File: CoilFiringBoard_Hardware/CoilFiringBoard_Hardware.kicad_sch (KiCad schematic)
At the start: 16 parts, among them Q1 Q_NMOS_GDS, Q2 Q_NMOS_GDS

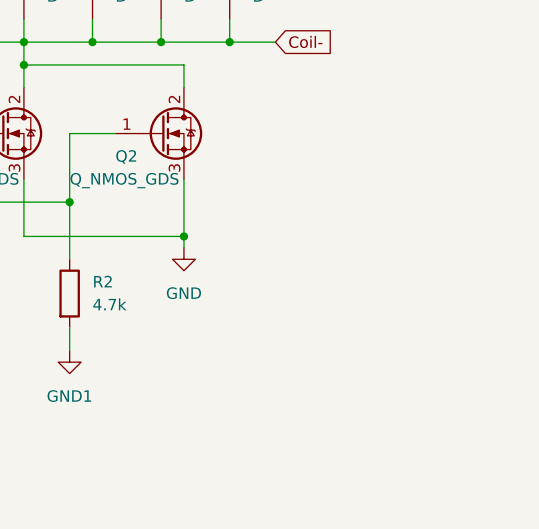
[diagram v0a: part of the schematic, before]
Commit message: Updated layout
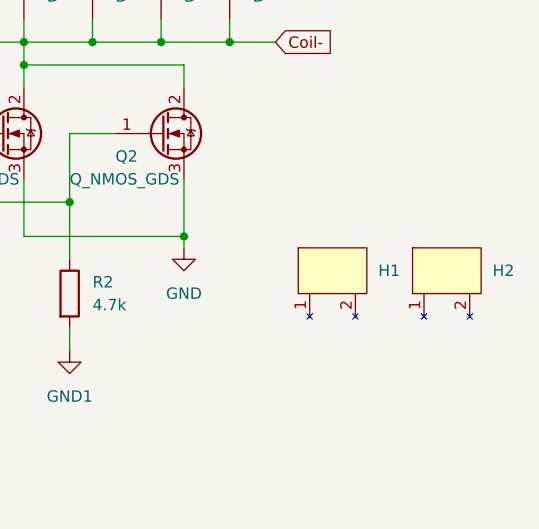
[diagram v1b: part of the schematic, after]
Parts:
- added H1, H2: ~, SeniorDesign:WV-T264-101E, symbol SeniorDesign:WV-T264-101E
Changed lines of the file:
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@@
+    )
+  )
+  (symbol (lib_id "SeniorDesign:WV-T264-101E") (at 180.34 99.06 0) (unit 1)
+    (in_bom yes) (on_board yes) (dnp no) (fields_autoplaced)
+    (property "Reference" "H1" (at 185.42 99.06 0)
+      (effects (font (size 1.27 1.27)) (justify left))
+    )
+    (property "Value" "~" (at 180.34 99.06 0)
+      (effects (font (size 1.27 1.27)))
+    )
+    (property "Footprint" "SeniorDesign:WV-T264-101E" (at 180.34 99.06 0)
+      (effects (font (size 1.27 1.27)) hide)
+    )
+    (property "Datasheet" "" (at 180.34 99.06 0)
+      (effects (font (size 1.27 1.27)) hide)
+    )
+    (pin "1")
+    (pin "2")
+    (instances
+      (project "CoilFiringBoard_Hardware"
+        (path "/28c13569-1eb8-4279-9ec4-13288f6f9832"
+          (reference "H1") (unit 1)
+        )
+      )
     )
   )
@@
         )
       )
+    )
+  )
+  (symbol (lib_id "SeniorDesign:WV-T264-101E") (at 193.04 99.06 0) (unit 1)
+    (in_bom yes) (on_board yes) (dnp no) (fields_autoplaced)
+    (property "Reference" "H2" (at 198.12 99.06 0)
+      (effects (font (size 1.27 1.27)) (justify left))
+    )
+    (property "Value" "~" (at 193.04 99.06 0)
+      (effects (font (size 1.27 1.27)))
+    )
+    (property "Footprint" "SeniorDesign:WV-T264-101E" (at 193.04 99.06 0)
+      (effects (font (size 1.27 1.27)) hide)
+    )
+    (property "Datasheet" "" (at 193.04 99.06 0)
+      (effects (font (size 1.27 1.27)) hide)
+    )
+    (pin "1")
+    (pin "2")
+    (instances
+      (project "CoilFiringBoard_Hardware"
+        (path "/28c13569-1eb8-4279-9ec4-13288f6f9832"
+          (reference "H2") (unit 1)
+        )
+      )

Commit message: Changed cap footprint
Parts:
- C1: footprint Capacitor_THT:C_Disc_D10.5mm_W5.0mm_P10.00mm -> Capacitor_THT:C_Rect_L13.0mm_W5.0mm_P10.00mm_FKS3_FKP3_MKS4
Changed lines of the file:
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@@
       (effects (font (size 1.27 1.27)))
     )
-    (property "Footprint" "Capacitor_THT:C_Disc_D10.5mm_W5.0mm_P10.00mm" (at 123.19 115.8748 0)
+    (property "Footprint" "Capacitor_THT:C_Rect_L13.0mm_W5.0mm_P10.00mm_FKS3_FKP3_MKS4" (at 123.19 115.8748 0)
       (effects (font (size 1.27 1.27)) hide)
     )
